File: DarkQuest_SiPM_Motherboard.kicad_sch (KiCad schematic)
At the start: 46 parts, among them J1 Conn_Coaxial, J10 Conn_Coaxial, J11 Conn_Coaxial, J12 Conn_Coaxial, J13 8-102202-4, J14 8-102202-4, J15 8-102202-4, J16 8-102202-4, J17 SiPM Chip Pin Header (K), J18 SiPM Chip Pin Header (K)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

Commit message: Finished initial routing
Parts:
- removed J1, J10, J11, J12, J2, J3, J4, J9: Conn_Coaxial, Connector_Coaxial:WR-MMCX_Wuerth_66012102111404_Vertical, symbol Connector:Conn_Coaxial
- removed J13, J14, J15, J16: 8-102202-4, Connector_PinHeader_2.54mm:PinHeader_1x03_P2.54mm_Vertical, symbol Connector:Conn_01x03_Female
- removed J17, J18, J19, J20: SiPM Chip Pin Header (K), Connector_PinHeader_2.54mm:PinHeader_1x10_P2.54mm_Vertical, symbol Connector:Conn_01x10_Pin
- removed J5, J6, J7, J8: SiPM Chip Pin Header (A), Connector_PinHeader_2.54mm:PinHeader_1x10_P2.54mm_Vertical, symbol Connector:Conn_01x10_Pin
- removed JP1, JP2, JP3, JP4: SolderJumper_2_Open, Jumper:SolderJumper-2_P1.3mm_Open_RoundedPad1.0x1.5mm, symbol Jumper:SolderJumper_2_Open
- removed SW1, SW2, SW3, SW4: SW_Push_DPDT, Relay_SMD:Nidec_DPDT_CS422YTA, symbol Switch:Nidec_DPDT
- removed U1, U2, U3, U4: ~, Resistor_SMD:D10AA20Z4, symbol Analog:D10AA20Z4
- renumbered J21 to J1, J23 to J2, J22 to J3, J24 to J4, J25 to J5
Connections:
- net A2_PreAtten is gone; now on net A1: J3.1 (Anode)
- net A3_PreAtten is gone; now on net A2: J4.1 (Anode)
- net A4 is gone; now on net A3: J1.8
- net A4_PreAtten is gone; now on net A3: J5.1 (Anode)
- net A1: now also J1.6; no longer J1.2
- net A2: now also J1.4; no longer J1.6
- net A3: no longer J1.4
- net K1: now also C2.1, J1.3, J3.3 (Cathode); no longer C1.2, J1.1, J2.3 (Cathode)
- net K2: now also C3.1, J1.5, J4.3 (Cathode); no longer C2.2, J1.3, J3.3 (Cathode)
- net K3: now also C4.1, J1.7, J5.3 (Cathode); no longer C3.2, J1.5, J4.3 (Cathode)
- net GND: now reaches J1.SH
- net GND: now also C1.2, C2.2, C3.2, C4.2, J2.2 (GND), J3.2 (GND), J4.2 (GND), J5.2 (GND)
- net A1_PreAtten renamed A0
- net A0: now also J1.2
- net GND1 renamed K0
- net K0: now also J1.1, J2.3 (Cathode); no longer J2.2 (GND)
- removed net GND2: C2.1, J3.2 (GND)
- removed net GND3: C3.1, J4.2 (GND)
- removed net GND4: C4.1, J5.2 (GND)
- removed net K4: C4.2, J1.7, J5.3 (Cathode)
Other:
- moved on the sheet: C3, J1, J2, J3, J4, J5

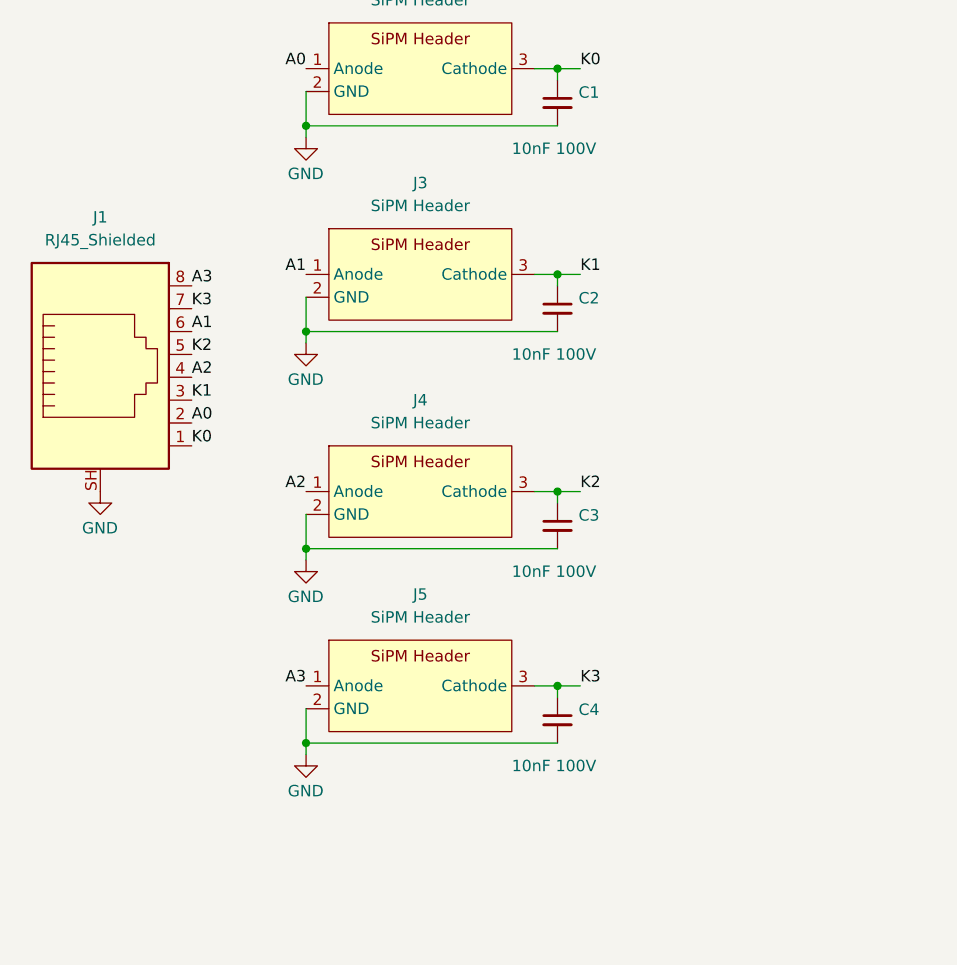
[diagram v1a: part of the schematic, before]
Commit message: Dual RJ45 Solution
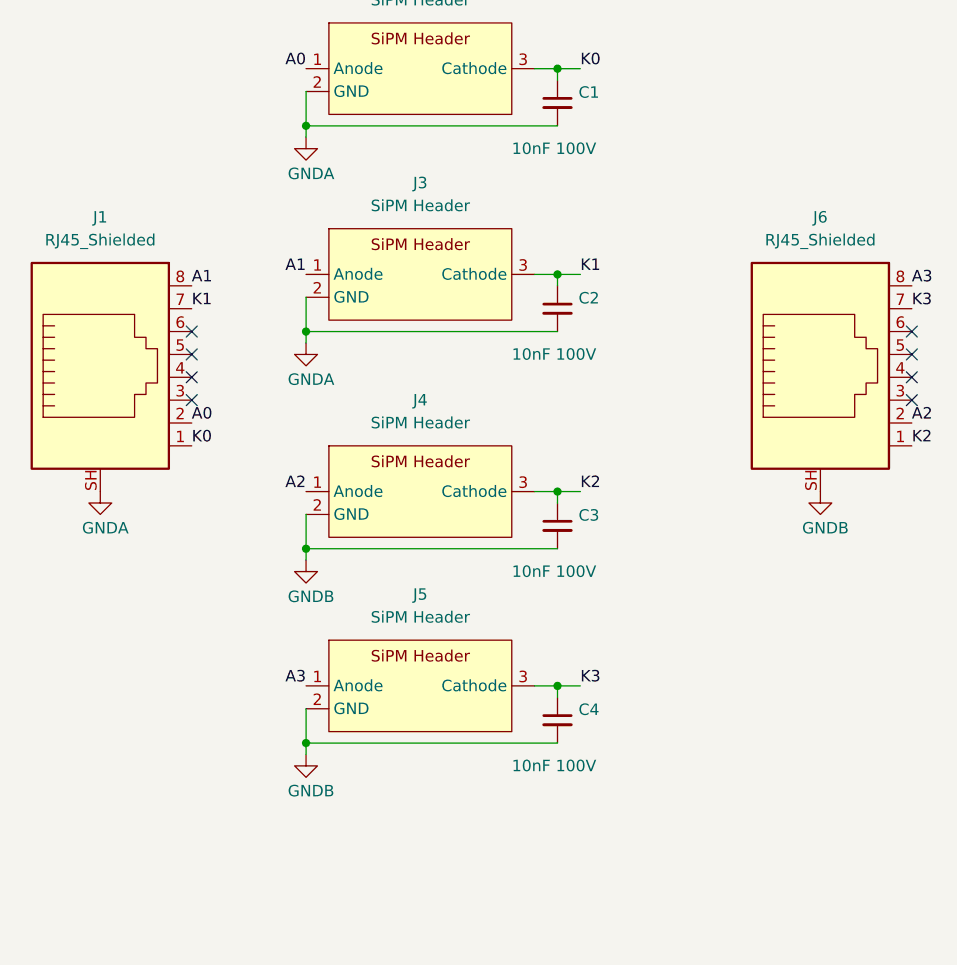
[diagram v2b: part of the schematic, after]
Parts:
- added J6: RJ45_Shielded, RJJS-88-122-E7V-022:RJJS-88-122-E7V-022, symbol Connector:RJ45_Shielded
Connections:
- net A1: now also J1.8; no longer J1.6
- net A2: now also J6.2; no longer J1.4
- net A3: now also J6.8; no longer J1.8
- net K1: now also J1.7; no longer J1.3
- net K2: now also J6.1; no longer J1.5
- net K3: now also J6.7; no longer J1.7
- net GND renamed GNDA
- net GNDA: no longer C3.2, C4.2, J4.2 (GND), J5.2 (GND)
- new net GNDB: C3.2, C4.2, J4.2 (GND), J5.2 (GND), J6.SH
- no-connect marks 0 -> 8
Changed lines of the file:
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@@
 		(color 0 0 0 0)
+	)
+	(no_connect
+		(at 38.1 60.96)
+	)
+	(no_connect
+		(at 38.1 66.04)
+	)
+	(no_connect
+		(at 118.11 66.04)
+	)
+	(no_connect
+		(at 38.1 63.5)
+	)
+	(no_connect
+		(at 118.11 60.96)
+	)
+	(no_connect
+		(at 118.11 68.58)
+	)
+	(no_connect
+		(at 118.11 63.5)
+	)
+	(no_connect
+		(at 38.1 68.58)
 	)
 	(wire
@@
 	)
 	(label "K2"
-		(at 38.1 63.5 0)
-		(effects
-			(font
-				(size 1.27 1.27)
-			)
-			(justify left bottom)
-		)
-	)
-	(label "A1"
-		(at 38.1 60.96 0)
+		(at 118.11 73.66 0)
 		(effects
 			(font
@@
 		)
 	)
+	(label "A2"
+		(at 118.11 71.12 0)
+		(effects
+			(font
+				(size 1.27 1.27)
+			)
+			(justify left bottom)
+		)
+	)
+	(label "K1"
+		(at 38.1 58.42 0)
+		(effects
+			(font
+				(size 1.27 1.27)
+			)
+			(justify left bottom)
+		)
+	)
+	(label "K3"
+		(at 118.11 58.42 0)
+		(effects
+			(font
+				(size 1.27 1.27)
+			)
+			(justify left bottom)
+		)
+	)
 	(label "A3"
 		(at 50.8 100.33 180)
@@
 	)
 	(label "A3"
-		(at 38.1 55.88 0)
-		(effects
-			(font
-				(size 1.27 1.27)
-			)
-			(justify left bottom)
-		)
-	)
-	(label "K3"
-		(at 38.1 58.42 0)
-		(effects
-			(font
-				(size 1.27 1.27)
-			)
-			(justify left bottom)
-		)
-	)
-	(label "K1"
-		(at 38.1 68.58 0)
+		(at 118.11 55.88 0)
 		(effects
 			(font
@@
 		)
 	)
-	(label "A2"
-		(at 38.1 66.04 0)
+	(label "A1"
+		(at 38.1 55.88 0)
 		(effects
 			(font
@@
 			)
 		)
-		(property "Value" "GND"
+		(property "Value" "GNDA"
 			(at 25.908 82.804 0)
 			(effects
@@
 	(symbol
 		(lib_id "power:GND1")
+		(at 107.95 78.74 0)
+		(unit 1)
+		(exclude_from_sim no)
+		(in_bom yes)
+		(on_board yes)
+		(dnp no)
+		(property "Reference" "#PWR06"
+			(at 107.95 85.09 0)
+			(effects
+				(font
+					(size 1.27 1.27)
+				)
+				(hide yes)
+			)
+		)
+		(property "Value" "GNDB"
+			(at 105.918 82.804 0)
+			(effects
+				(font
+					(size 1.27 1.27)
+				)
+				(justify left)
+			)
+		)
+		(property "Footprint" ""
+			(at 107.95 78.74 0)
+			(effects
+				(font
+					(size 1.27 1.27)
+				)
+				(hide yes)
+			)
+		)
+		(property "Datasheet" ""
+			(at 107.95 78.74 0)
+			(effects
+				(font
+					(size 1.27 1.27)
+				)
+				(hide yes)
+			)
+		)
+		(property "Description" "Power symbol creates a global label with name \"GND1\" , ground"
+			(at 107.95 78.74 0)
+			(effects
+				(font
+					(size 1.27 1.27)
+				)
+				(hide yes)
+			)
+		)
+		(pin "1"
+		)
+		(instances
+			(project "DarkQuest_SiPM_Motherboard"
+				(path "/80df74f6-3cfc-4d0d-aa5e-7f4ce133cc92"
+					(reference "#PWR06")
+					(unit 1)
+				)
+			)
+		)
+	)
+	(symbol
+		(lib_id "power:GND1")
 		(at 50.8 39.37 0)
 		(unit 1)
@@
 			)
 		)
-		(property "Value" "GND"
+		(property "Value" "GNDA"
 			(at 48.768 43.434 0)
 			(effects
@@
 			)
 		)
-		(property "Value" "GND"
+		(property "Value" "GNDB"
 			(at 48.768 112.014 0)
 			(effects
@@
 			)
 		)
-		(property "Value" "GND"
+		(property "Value" "GNDA"
 			(at 48.768 66.294 0)
 			(effects
@@
 			)
 		)
-		(property "Value" "GND"
+		(property "Value" "GNDB"
 			(at 48.768 90.424 0)
 			(effects
@@
 					(unit 1)
 				)
+			)
+		)
+	)
+	(symbol
+		(lib_id "Connector:RJ45_Shielded")
+		(at 107.95 66.04 0)
+		(unit 1)
+		(exclude_from_sim no)
+		(in_bom yes)
+		(on_board yes)
+		(dnp no)
+		(fields_autoplaced yes)
+		(property "Reference" "J6"
+			(at 107.95 48.26 0)
+			(effects
+				(font
+					(size 1.27 1.27)
+				)
+			)
+		)
+		(property "Value" "RJ45_Shielded"
+			(at 107.95 50.8 0)
+			(effects
+				(font
+					(size 1.27 1.27)
+				)
+			)
+		)
+		(property "Footprint" "RJJS-88-122-E7V-022:RJJS-88-122-E7V-022"
+			(at 107.95 65.405 90)
+			(effects
+				(font
+					(size 1.27 1.27)
+				)
+				(hide yes)
+			)
+		)
+		(property "Datasheet" "~"
+			(at 107.95 65.405 90)
+			(effects
+				(font
+					(size 1.27 1.27)
+				)
+				(hide yes)
+			)
+		)
+		(property "Description" "RJ connector, 8P8C (8 positions 8 connected), Shielded"
+			(at 107.95 66.04 0)
+			(effects
+				(font
+					(size 1.27 1.27)
+				)
+				(hide yes)
+			)
+		)
+		(pin "5"
+		)
+		(pin "4"
+		)
+		(pin "3"
+		)
+		(pin "8"
+		)
+		(pin "SH"
+		)
+		(pin "2"
+		)
+		(pin "7"
+		)
+		(pin "6"
+		)
+		(pin "1"
+		)
+		(instances
+			(project "DarkQuest_SiPM_Motherboard"
+				(path "/80df74f6-3cfc-4d0d-aa5e-7f4ce133cc92"
+					(reference "J6")
+					(unit 1)
+				)
